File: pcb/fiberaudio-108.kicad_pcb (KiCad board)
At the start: 2 copper layers, 45 x 45 mm, 43 parts, among them J1 USB_B_Mini, J2 PLT133_T10W, Q1 SI2301CDS, SW1 MUTE, U1 AT93C46D, U2 CM108AH, U3 SRV05-4, Y1 12MHz

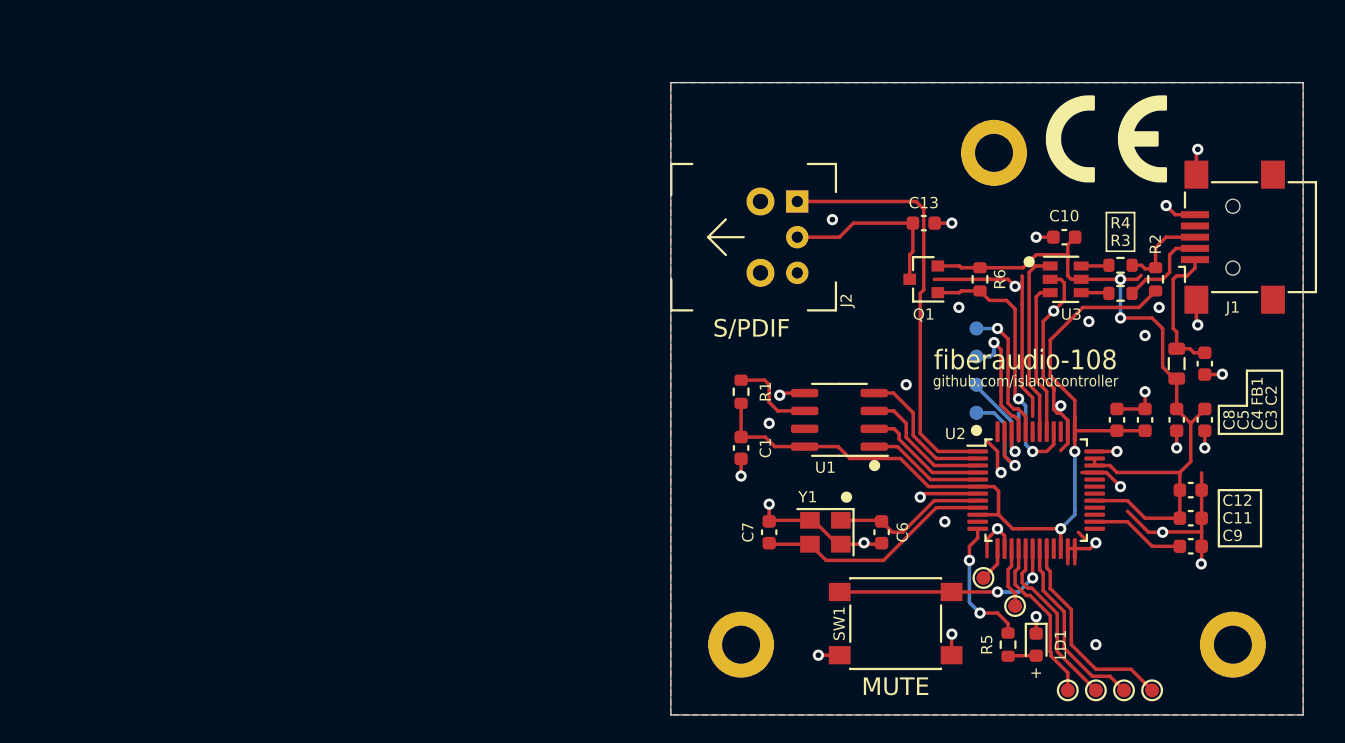
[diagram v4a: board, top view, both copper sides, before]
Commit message: Adjust thermal relief to help prevent tombstoning
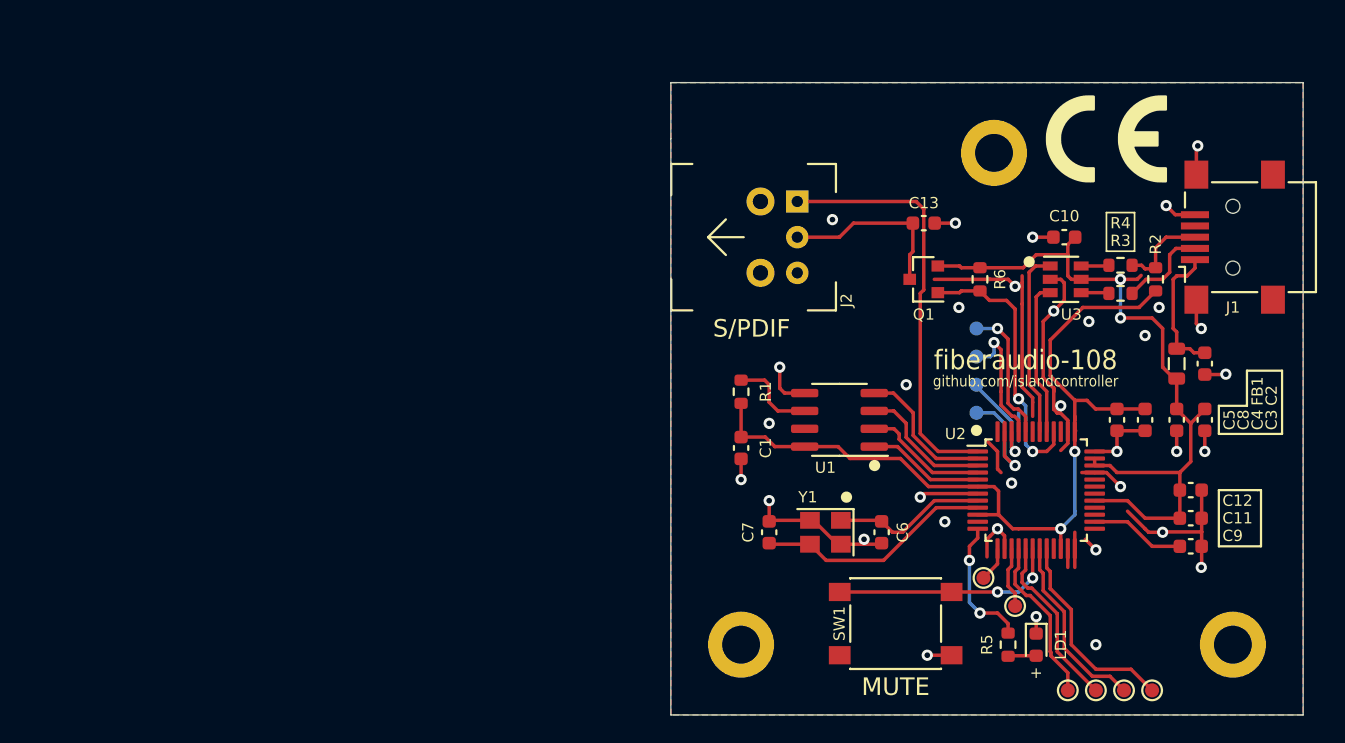
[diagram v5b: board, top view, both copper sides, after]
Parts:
- moved C5 2.00 mm to (133.8, 65.0), turned to 270 degrees
- moved C8 2.00 mm to (135.8, 65.0), turned to 270 degrees
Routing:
- net GND: track 99.7 -> 101.5 mm, vias 36 -> 34
